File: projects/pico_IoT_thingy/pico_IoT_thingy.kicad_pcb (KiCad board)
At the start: 2 copper layers, 58 parts, among them IC1 THVD1406DR, J1 Barrel_Jack_Switch, J2 QWIIC, J3 Conn_01x03, J4 Screw_Terminal_01x03, J5 Screw_Terminal_01x04, J6 Conn_02x05_Odd_Even, J7 Conn_01x02, K1 RT314A05, Q1 BC817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

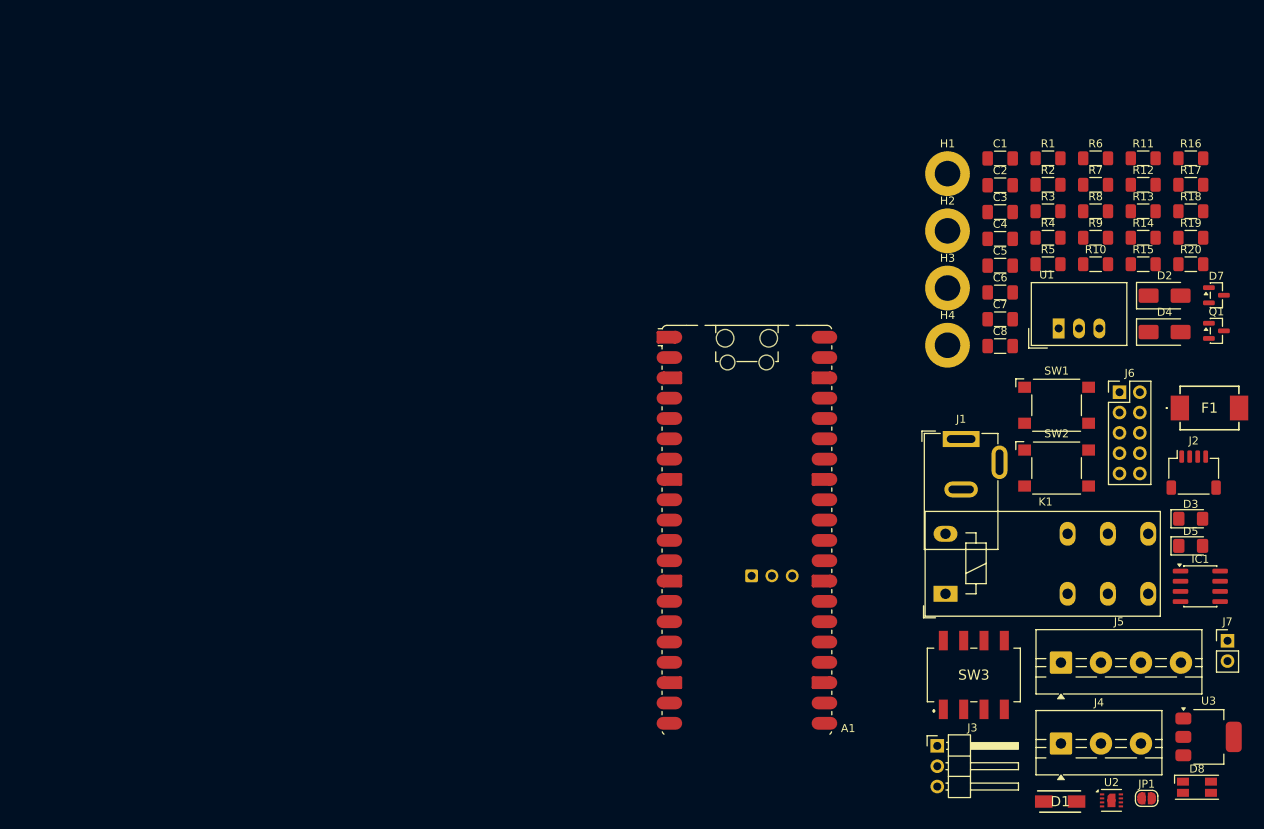
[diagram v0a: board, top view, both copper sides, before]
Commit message: Pico IoT thingy - initial placement of components in PCB
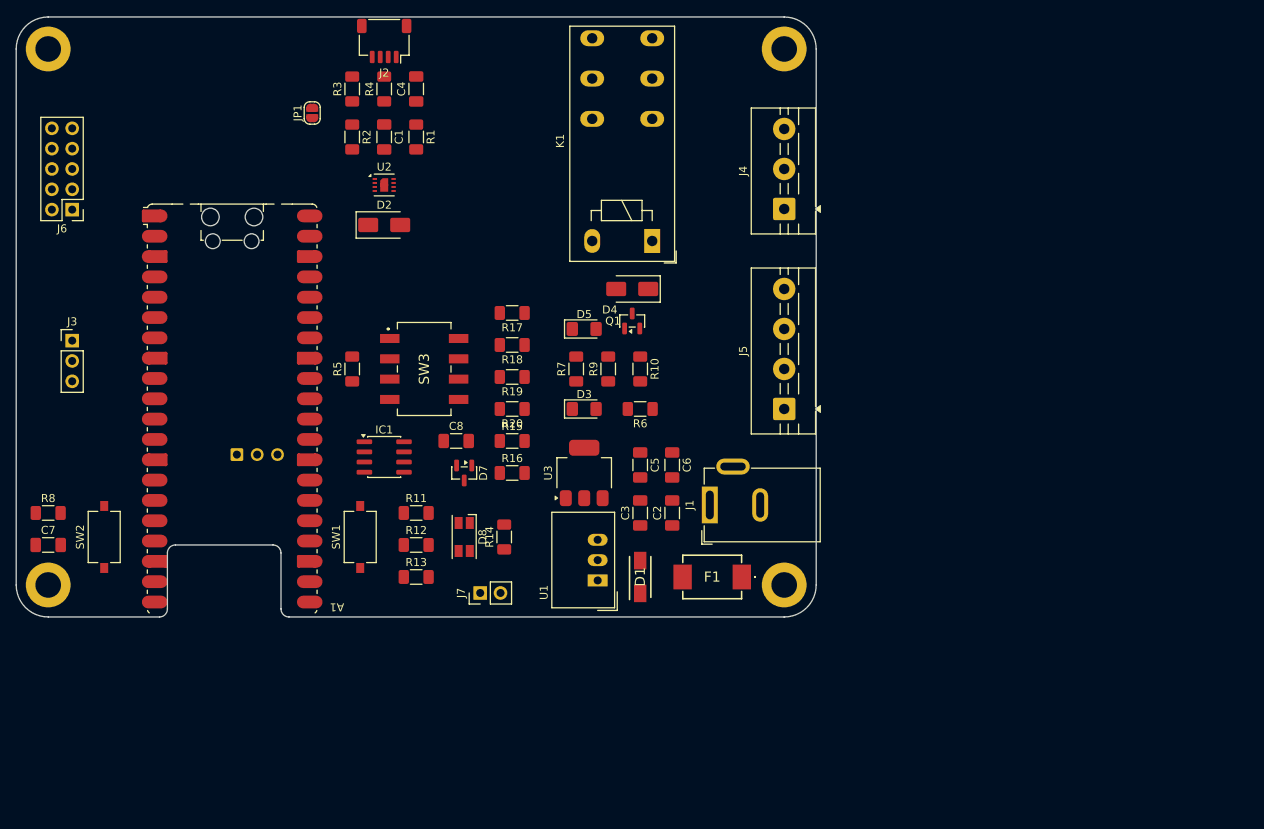
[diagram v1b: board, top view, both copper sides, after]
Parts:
- J3: footprint Connector_PinHeader_2.54mm:PinHeader_1x03_P2.54mm_Horizontal -> Connector_PinHeader_2.54mm:PinHeader_1x03_P2.54mm_Vertical
- SW1, SW2: footprint Button_Switch_SMD:SW_SPST_Omron_B3FS-101xP -> Button_Switch_SMD:SW_Tactile_SPST_NO_Straight_CK_PTS636Sx25SMTRLFS
- moved R8 136.2 mm to (44.0, 102.0)
- moved JP1 135.0 mm to (77.0, 52.0), turned to 90 degrees
- moved J6 132.9 mm to (47.0, 64.1), turned to 180 degrees
- moved C7 122.3 mm to (44.0, 106.0)
- moved J3 119.4 mm to (47.0, 80.5)
- moved SW2 119.4 mm to (51.0, 105.0), turned to 90 degrees
- moved U2 119.1 mm to (86.0, 61.0)
- moved H3 118.4 mm to (44.0, 111.0)
- moved J2 114.7 mm to (86.0, 43.0), turned to 180 degrees
- moved H1 113.5 mm to (44.0, 44.0)
- moved IC1 103.3 mm to (86.0, 95.0)
- moved R13 101.7 mm to (90.0, 110.0)
- moved R12 101.4 mm to (90.0, 106.0)
- moved R11 101.1 mm to (90.0, 102.0)
- moved D2 97.9 mm to (86.0, 66.0)
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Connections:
- J6 pad 1: +3V3 -> GND
- J6 pad 10: GND -> +3V3
- J6 pad 2: +3V3 -> GND
- J6 pad 3: /SPI0_TX -> /GPIO27
- J6 pad 4: /SPI0_CSn -> /SPI0_RX
- J6 pad 5: /SPI0_SCK -> /GPIO26
- J6 pad 6: /GPIO26 -> /SPI0_SCK
- J6 pad 7: /SPI0_RX -> /SPI0_CSn
- J6 pad 8: /GPIO27 -> /SPI0_TX
- J6 pad 9: GND -> +3V3
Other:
- board outline added: 100 x 75 mm

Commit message: Pico IoT thingy - Flip 1x04 screw terminal to have GND on Pin 1, add 3Ds
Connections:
- J5 pad 1: /B -> GND
- J5 pad 2: /A -> +5V
- J5 pad 3: +5V -> /A
- J5 pad 4: GND -> /B
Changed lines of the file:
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@@
 			)
 		)
+		(model "${KIPRJMOD}/libraries/MH_Screw_Terminals/Screw_Terminal_Block_1x03_P5mm.step"
+			(offset
+				(xyz -73 0 0)
+			)
+			(scale
+				(xyz 1 1 1)
+			)
+			(rotate
+				(xyz -180 -0 -0)
+			)
+		)
 	)
 	(footprint "MountingHole:MountingHole_3.2mm_M3_DIN965_Pad"
@@
 			(remove_unused_layers no)
 			(roundrect_rratio 0.089286)
-			(net 52 "/B")
+			(net 1 "GND")
 			(pinfunction "Pin_1")
 			(pintype "passive")
@@
 			(layers "*.Cu" "*.Mask")
 			(remove_unused_layers no)
-			(net 53 "/A")
+			(net 39 "+5V")
 			(pinfunction "Pin_2")
 			(pintype "passive")
@@
 			(layers "*.Cu" "*.Mask")
 			(remove_unused_layers no)
-			(net 39 "+5V")
+			(net 53 "/A")
 			(pinfunction "Pin_3")
 			(pintype "passive")
@@
 			(layers "*.Cu" "*.Mask")
 			(remove_unused_layers no)
-			(net 1 "GND")
+			(net 52 "/B")
 			(pinfunction "Pin_4")
 			(pintype "passive")
@@
 			)
 			(rotate
-				(xyz 0 0 0)
+				(xyz -0 -0 -0)
+			)
+		)
+		(model "${KIPRJMOD}/libraries/MH_Screw_Terminals/Screw_Terminal_Block_1x02_P5mm.step"
+			(offset
+				(xyz -41 0 0)
+			)
+			(scale
+				(xyz 1 1 1)
+			)
+			(rotate
+				(xyz -180 -0 -0)
+			)
+		)
+		(model "${KIPRJMOD}/libraries/MH_Screw_Terminals/Screw_Terminal_Block_1x02_P5mm.step"
+			(offset
+				(xyz -31 0 0)
+			)
+			(scale
+				(xyz 1 1 1)
+			)
+			(rotate
+				(xyz -180 -0 -0)
 			)
 		)

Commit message: Pico IoT thingy - logos and initial routing
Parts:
- added G***: LOGO, MH_logos:robot_duckie_logo_12mm, F.Cu at (67.0, 47.0)
- added REF**: MH_Symbol_HighVoltage_Triangle_8x7mm_Silkscreen, MH_logos:MH_Symbol_HighVoltage_Triangle_8x7mm_Silkscreen, F.Cu at (128.5, 45.5)
- added REF**: KiCad-Logo2_5mm_SilkScreen, Symbol:KiCad-Logo2_5mm_SilkScreen, F.Cu at (67.0, 57.0)
- moved J3 3.84 mm to (45.7, 76.8)
- moved D2 2.62 mm to (88.3, 67.3)
- moved U2 2.55 mm to (88.5, 61.5)
- moved C1 2.50 mm to (88.5, 55.0)
- moved C4 2.50 mm to (92.5, 49.0)
- moved J2 2.50 mm to (88.5, 43.0)
- moved JP1 2.50 mm to (79.5, 52.0)
- moved R1 2.50 mm to (92.5, 55.0)
- moved R2 2.50 mm to (84.5, 55.0)
- moved R3 2.50 mm to (84.5, 49.0)
- moved R4 2.50 mm to (88.5, 49.0)
- moved D4 1.41 mm to (116.0, 73.0)
- moved J6 1.26 mm to (48.3, 64.1)
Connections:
- net Net-(J4-Pin_1) renamed /LOAD_NC
- net Net-(J4-Pin_2) renamed /LOAD_COM
- net Net-(J4-Pin_3) renamed /LOAD_NO
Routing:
- net +3V3: track 0.00 -> 212.0 mm
- net +5V: track 0.00 -> 109.9 mm
- net GND: track 0.00 -> 73.7 mm
- net /GPIO26: track 0.00 -> 68.8 mm
- net /GPIO27: track 0.00 -> 41.0 mm
- net /SPI0_TX: track 0.00 -> 40.0 mm
- net /SPI0_CSn: track 0.00 -> 31.4 mm
- net /SPI0_RX: track 0.00 -> 20.8 mm
- net /SW: track 0.00 -> 19.2 mm
- net +24V: track 0.00 -> 19.1 mm
- net /SPI0_SCK: track 0.00 -> 19.0 mm
- net Net-(D4-A): track 0.00 -> 19.0 mm
- net Net-(JP1-A): track 0.00 -> 14.6 mm
- net /LED_G: track 0.00 -> 13.7 mm
- net /LED_R: track 0.00 -> 13.2 mm
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- added copper zone on B.Cu, net /LOAD_COM
- added copper zone on F.Cu, net /LOAD_COM
- added copper zone on B.Cu, net /LOAD_NC
- added copper zone on F.Cu, net /LOAD_NC
- added copper zone on B.Cu, net /LOAD_NO
- added copper zone on F.Cu, net /LOAD_NO
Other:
- outline, holes or cut-outs redrawn
- copper layers 2 -> 4
- board text added: "5V"
- board text added: "A-"
- board text added: "B+"
- board text added: "COM"
- board text added: "GND"
- board text added: "NC"
- board text added: "NO"

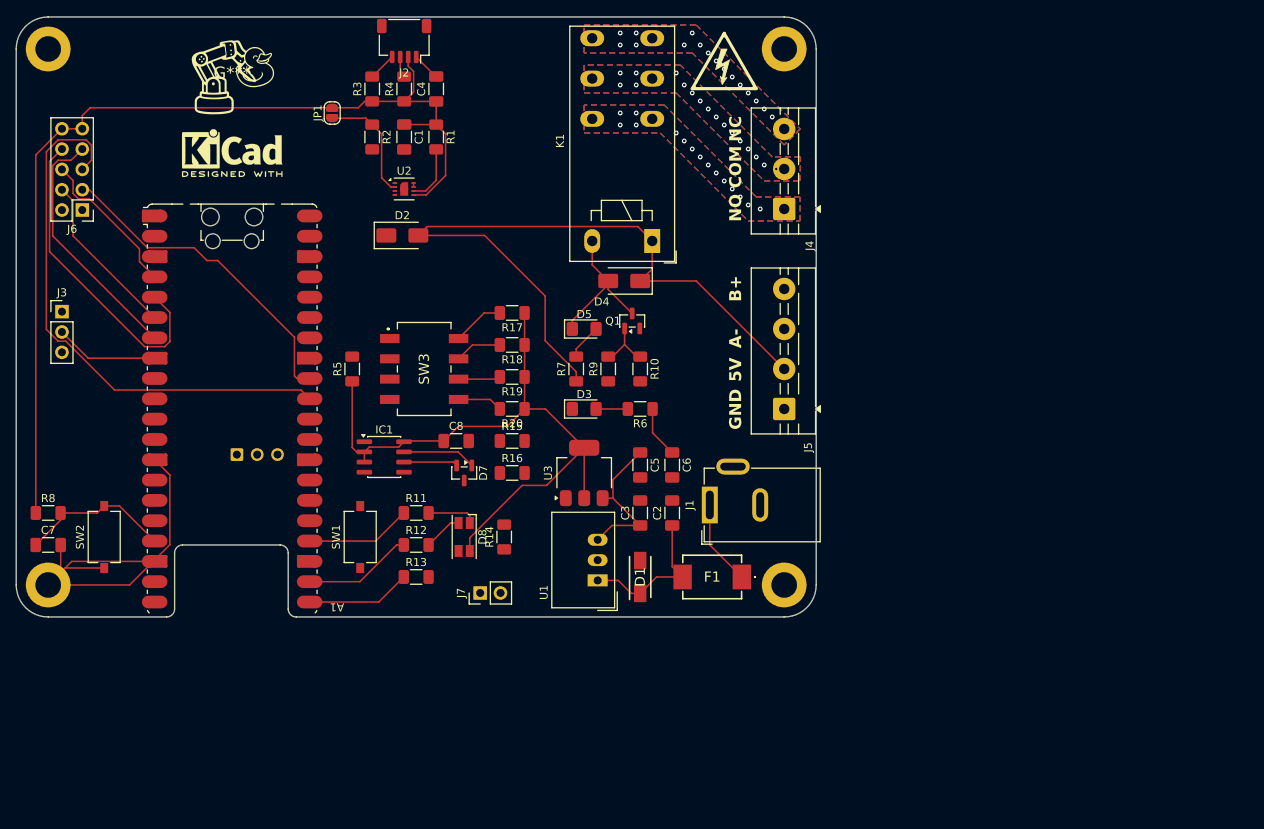
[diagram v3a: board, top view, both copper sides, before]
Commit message: Pico IoT thingy - remove initial routing, clean up silkscreen
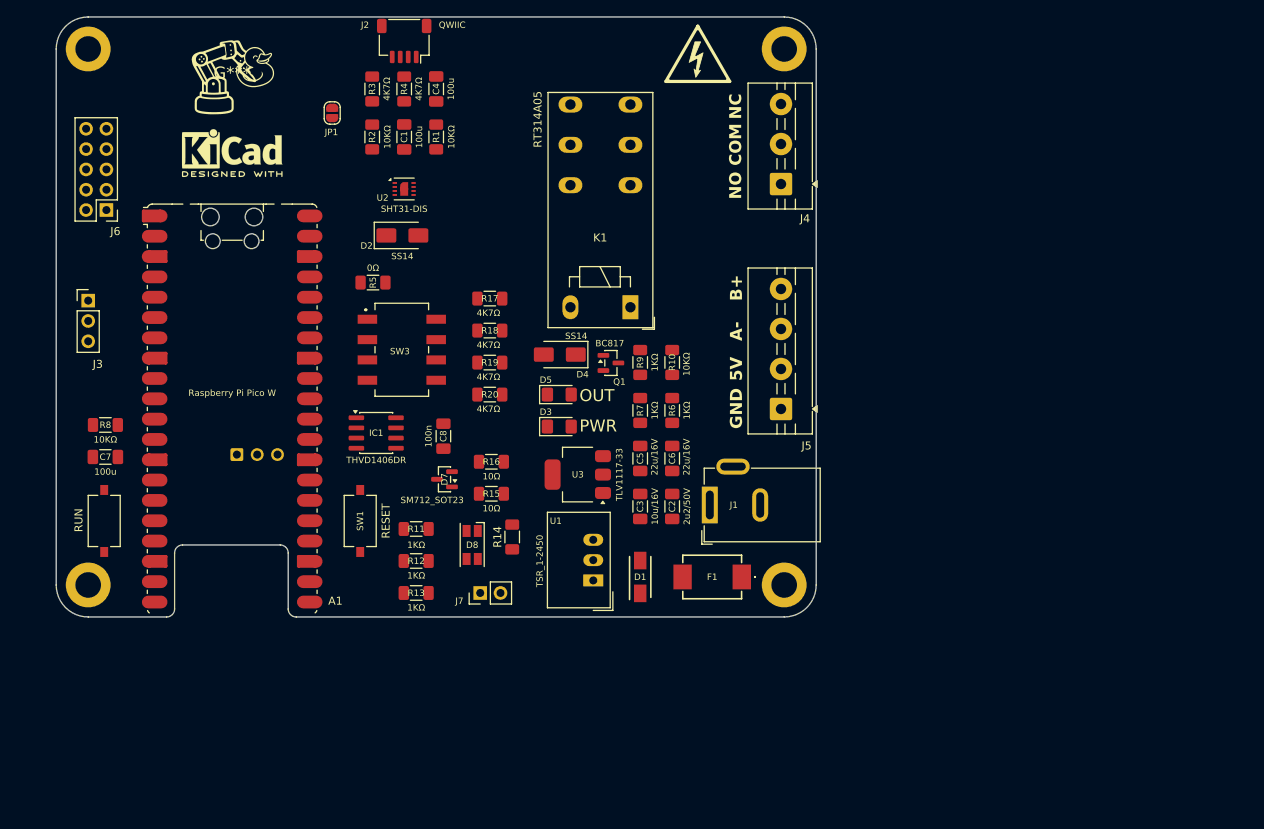
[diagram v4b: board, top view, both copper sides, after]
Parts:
- A1: value RaspberryPi_Pico_W -> Raspberry Pi Pico W
- moved C7 13.1 mm to (51.1, 95.0)
- moved R8 13.1 mm to (51.1, 91.0)
- moved D4 12.2 mm to (108.0, 82.2)
- moved R5 11.1 mm to (84.6, 73.2), turned to 180 degrees
- moved R7 9.53 mm to (118.0, 89.2)
- moved D5 8.77 mm to (107.9, 87.2)
- moved K1 8.72 mm to (116.8, 76.3)
- moved R15 7.09 mm to (99.4, 99.6)
- moved Q1 5.89 mm to (114.3, 83.2), turned to 0 degrees
- moved H1 5.00 mm to (49.0, 44.0)
- moved H3 5.00 mm to (49.0, 111.0)
- moved R10 4.08 mm to (122.0, 83.2)
- moved R9 4.08 mm to (118.0, 83.2)
- moved R6 4.00 mm to (122.0, 89.2), turned to 90 degrees
- moved D3 3.81 mm to (107.9, 91.2)
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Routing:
- net +3V3: track 212.0 -> 0.00 mm
- net +5V: track 109.9 -> 0.00 mm
- net GND: track 73.7 -> 0.00 mm
- net /GPIO26: track 68.8 -> 0.00 mm
- net /GPIO27: track 41.0 -> 0.00 mm
- net /SPI0_TX: track 40.0 -> 0.00 mm
- net /SPI0_CSn: track 31.4 -> 0.00 mm
- net /SPI0_RX: track 20.8 -> 0.00 mm
- net /SW: track 19.2 -> 0.00 mm
- net +24V: track 19.1 -> 0.00 mm
- net /SPI0_SCK: track 19.0 -> 0.00 mm
- net Net-(D4-A): track 19.0 -> 0.00 mm
- net Net-(JP1-A): track 14.6 -> 0.00 mm
- net /LED_G: track 13.7 -> 0.00 mm
- net /LED_R: track 13.2 -> 0.00 mm
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- removed copper zone on B.Cu, net /LOAD_COM
- removed copper zone on F.Cu, net /LOAD_COM
- removed copper zone on B.Cu, net /LOAD_NC
- removed copper zone on F.Cu, net /LOAD_NC
- removed copper zone on B.Cu, net /LOAD_NO
- removed copper zone on F.Cu, net /LOAD_NO
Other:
- board size 100 x 75 mm -> 95 x 75 mm
- board text added: "OUT"
- board text added: "PWR"
- board text added: "RESET"
- board text added: "RUN"

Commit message: Pico IoT thingy v1.0 complete
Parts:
- A1: value Raspberry Pi Pico W -> RaspberryPi_Pico_W
- moved J2 0.58 mm to (88.5, 43.6)
- moved C1 0.48 mm to (88.5, 55.5)
- moved C4 0.48 mm to (92.5, 49.5)
- moved JP1 0.48 mm to (79.5, 52.5)
- moved R1 0.48 mm to (92.5, 55.5)
- moved R2 0.48 mm to (84.5, 55.5)
- moved R3 0.48 mm to (84.5, 49.5)
- moved R4 0.48 mm to (88.5, 49.5)
- moved U2 0.48 mm to (88.5, 62.0)
- moved A1 0.10 mm to (67.0, 89.1)
- turned C7 to 180 degrees
- renumbered REF** to HIGHVOLT_LOGO, REF** to KICAD_LOGO
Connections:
- H2 pad 1: GND -> unconnected-(H2-Pad1)
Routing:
- net GND: track 0.00 -> 99.2 mm, vias 0 -> 24
- net +5V: track 0.00 -> 97.9 mm, vias 0 -> 2
- net /I2C1_SCL: track 0.00 -> 73.4 mm, vias 0 -> 2
- net /RELAY: track 0.00 -> 67.6 mm, vias 0 -> 2
- net /I2C1_SDA: track 0.00 -> 58.0 mm, vias 0 -> 2
- net /B: track 0.00 -> 47.6 mm, vias 0 -> 1
- net /GPIO26: track 0.00 -> 45.3 mm, vias 0 -> 1
- net +3V3: track 0.00 -> 44.7 mm, vias 0 -> 19
- net /A: track 0.00 -> 43.3 mm, vias 0 -> 1
- net /GPIO27: track 0.00 -> 42.9 mm
- net /UART0_TX: track 0.00 -> 40.6 mm, vias 0 -> 2
- net /DIP1: track 0.00 -> 35.2 mm
- net /SPI0_CSn: track 0.00 -> 35.1 mm
- net /UART0_RX: track 0.00 -> 34.6 mm, vias 0 -> 2
- net Net-(D7-A2): track 0.00 -> 33.1 mm
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- added copper zone on In2.Cu, net +3V3
- added copper zone on B.Cu, net /LOAD_COM
- added copper zone on F.Cu, net /LOAD_COM
- added copper zone on B.Cu, net /LOAD_NC
- added copper zone on F.Cu, net /LOAD_NC
- added copper zone on B.Cu, net /LOAD_NO
- added copper zone on F.Cu, net /LOAD_NO
- added copper zone on B.Cu, net GND
